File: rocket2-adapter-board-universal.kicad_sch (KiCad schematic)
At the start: 13 parts, among them J2 Conn_01x04_Socket, J3 Conn_01x02_Socket, J4 Conn_01x04_Socket, J5 DSUB_15pin/VGA Veritical Fema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

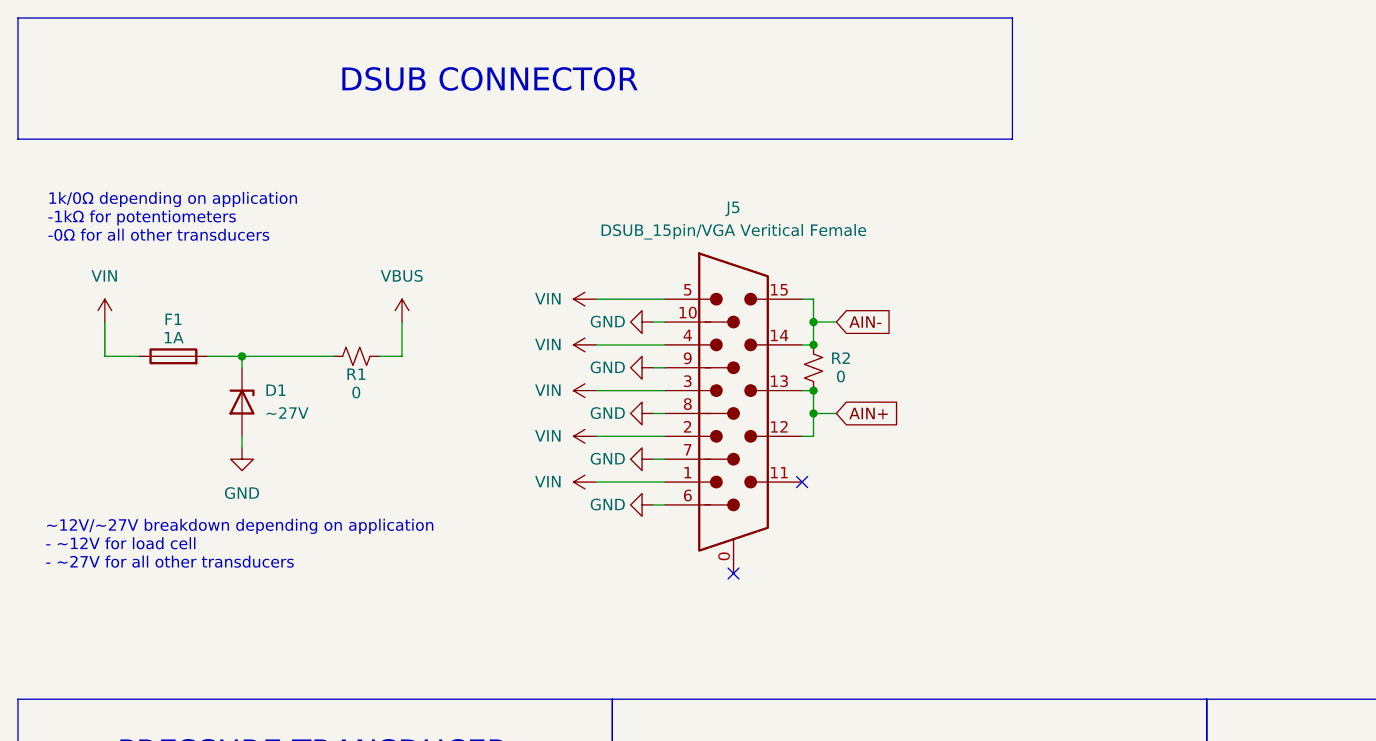
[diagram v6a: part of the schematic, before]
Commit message: Fixed resistor value/comments for POTs config
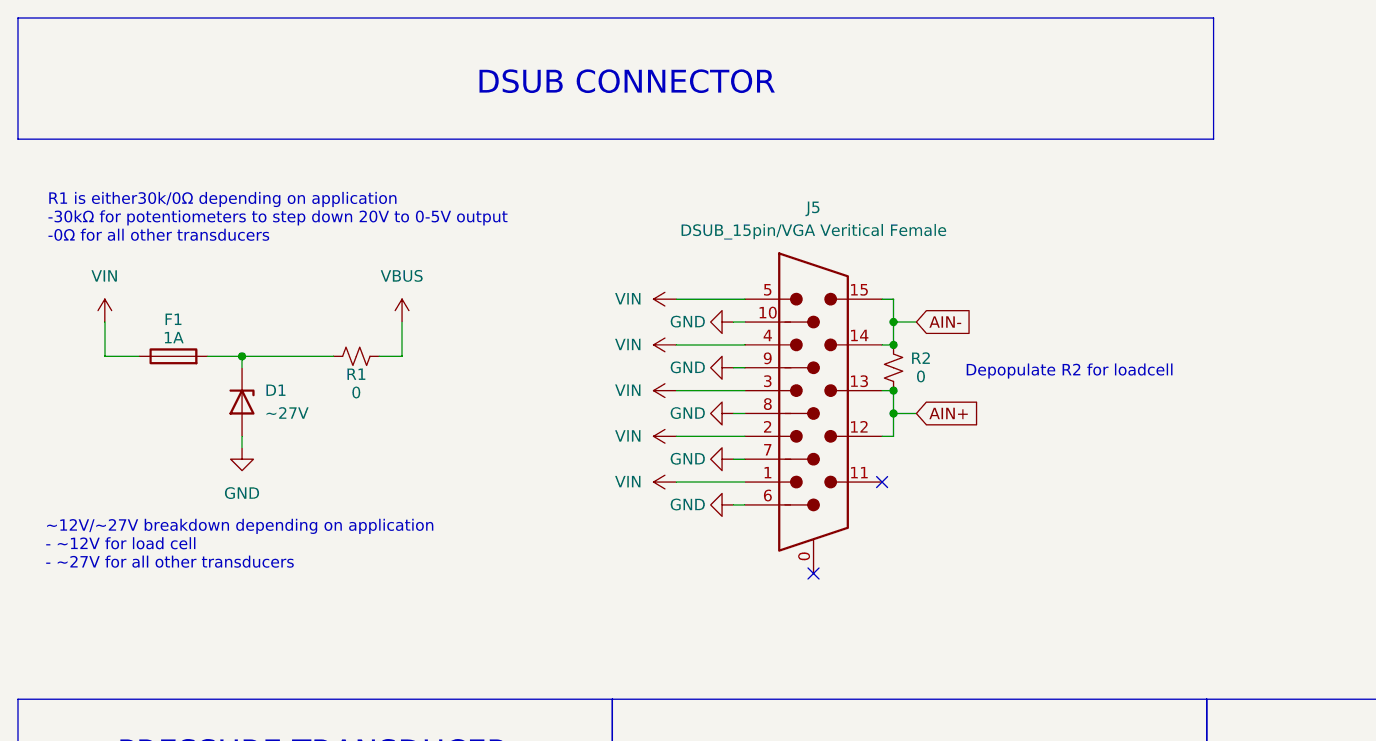
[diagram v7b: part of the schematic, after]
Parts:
- R1: Alt. Digikey Link SR0603JR-7T1KL -> ERA-3AEB303V; Alt. MPN https://www.digikey.com/en/products/detail/yageo/SR0603JR-7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 -> https://www.digikey.com/en/products/detail/panasonic-indust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; Alt. Manufacturer YAGEO -> Panasonic Industry
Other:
- note added: "Depopulate R2 for loadcell"
- note added: "R1 is either30k/0Ω depending on application -30kΩ for potentiometers to step down 20V to 0-5V output -0Ω for all other transducers"
- note removed: "1k/0Ω depending on application -1kΩ for potentiometers -0Ω for all other transducers"
- moved on the sheet: J5, R2
